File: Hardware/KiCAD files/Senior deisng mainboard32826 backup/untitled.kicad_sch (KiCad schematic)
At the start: 2 parts, among them U4 ESP32-S3-WROOM-2, U9 ESP32-S3-DevKitC

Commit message: Schematic adjustments made prior to initial submission to Chan thursday
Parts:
- removed U4: ESP32-S3-WROOM-2, PCM_Espressif:ESP32-S3-WROOM-2, symbol PCM_Espressif:ESP32-S3-WROOM-2
- removed U9: ESP32-S3-DevKitC, PCM_Espressif:ESP32-S3-DevKitC, symbol PCM_Espressif:ESP32-S3-DevKitC
- added J3: Rasberry Uart Conn_01x02, PCM_SparkFun-Connector:1x02_P2.54mm, symbol PCM_SparkFun-Connector:Conn_01x02_P2.54mm
- added U4: STM32H750VBTx, Package_QFP:LQFP-100_14x14mm_P0.5mm, symbol PCM_SparkFun-IC-Microcontroller:STM32H750VBTx
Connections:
- new net: U4.10 (VSS), U4.26 (VSS), U4.49 (VSS), U4.74 (VSS), U4.99 (VSS)
- new net VDD: U4.100 (VDD), U4.11 (VDD), U4.27 (VDD), U4.50 (VDD), U4.75 (VDD)

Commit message: MCU power, new MCU placed, LCD communication, AC coupling of voltage reg on MCU
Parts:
- removed U4: STM32H750VBTx, Package_QFP:LQFP-100_14x14mm_P0.5mm, symbol PCM_SparkFun-IC-Microcontroller:STM32H750VBTx
- added C13: 10uF, PCM_SparkFun-Capacitor:C_0805_2012Metric, symbol PCM_SparkFun-Capacitor:10uF_0805_25V_10%
- added C14: 0.1uF, PCM_SparkFun-Capacitor:C_0603_1608Metric, symbol PCM_SparkFun-Capacitor:0.1uF_0603_25V_20%
- added C16: 1.0uF, PCM_SparkFun-Capacitor:C_0402_1005Metric, symbol PCM_SparkFun-Capacitor:1.0uF_0402_16V_10%
- added IC1: STM32H723ZGT6, QFP50P2200X2200X160-144N, symbol STM32H723ZGT6:STM32H723ZGT6
- added SW5: SPDT_Slide_PTH_11.6x4.0mm, PCM_SparkFun-Switch:Slide_SPDT_PTH_11.6x4.0mm, symbol PCM_SparkFun-Switch:SPDT_Slide_PTH_11.6x4.0mm
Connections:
- net LPUART_RX: now reaches J3.1 (Pin_1)
- net LPUART_RX: now also IC1.102 (PA10)
- net LPUART_TX: now reaches J3.2 (Pin_2)
- net LPUART_TX: now also IC1.101 (PA9)
- new net: C13.2, C14.2
- new net +3.3V: C13.1, C14.1, C16.2, IC1.108 (VDD_8), IC1.121 (VDD_9), IC1.131 (VDD_10), IC1.144 (VDD_11), IC1.17 (VDD_1), IC1.30 (VDD_2), IC1.32 (VREF+), IC1.33 (VDDA), IC1.39 (VDD_3), IC1.52 (VDD_4), IC1.6 (VBAT), IC1.62 (VDD_5), IC1.72 (VDD_6), IC1.84 (VDD_7)
- new net CS: IC1.28 (PC2_C)
- new net GND: C16.1, IC1.107 (VSS_7), IC1.120 (VSS_8), IC1.130 (VSS_9), IC1.16 (VSS_1), IC1.31 (VSSA), IC1.38 (VSS_2), IC1.51 (VSS_3), IC1.61 (VSS_4), IC1.83 (VSS_5), IC1.94 (VSS_6)
- new net LCD_CLK: IC1.67 (PE14)
- new net MISO_4: IC1.4 (PE5)
- new net MOSI_4: IC1.5 (PE6)
- new net SPI4_SCK: IC1.1 (PE2)
- no-connect marks 0 -> 2
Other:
- note added: "100ma max"
- note added: "20ma max gpio"
- note added: "AC COUPPLING --- may not be neccesary"
- note added: "COME BACK AND VERIFY VOLTAGE REGULATION OF EACH POWER INPUT VDD_X"
- note added: "KEEP VREF+ and VSSA cap as close as possible to chip"
- note added: "PDR_on is for voltage supervision, meant for low power applications"
- note added: "Reset switch"
- note added: "Supply rail must have 10 us/V fall time"
- note added: "VBAT pin should be connected to VDD."
- note added: "VDD33USB: allows the support of a VDD supply different from 3.3 V while powering the USB transceiver with 3.3V on VDD33USB."
- note added: "check if VDDA needs a diff voltage regulation"
- note added: "introduces voltage scaling and powering Vcore @ Vcap"
- moved on the sheet: J3

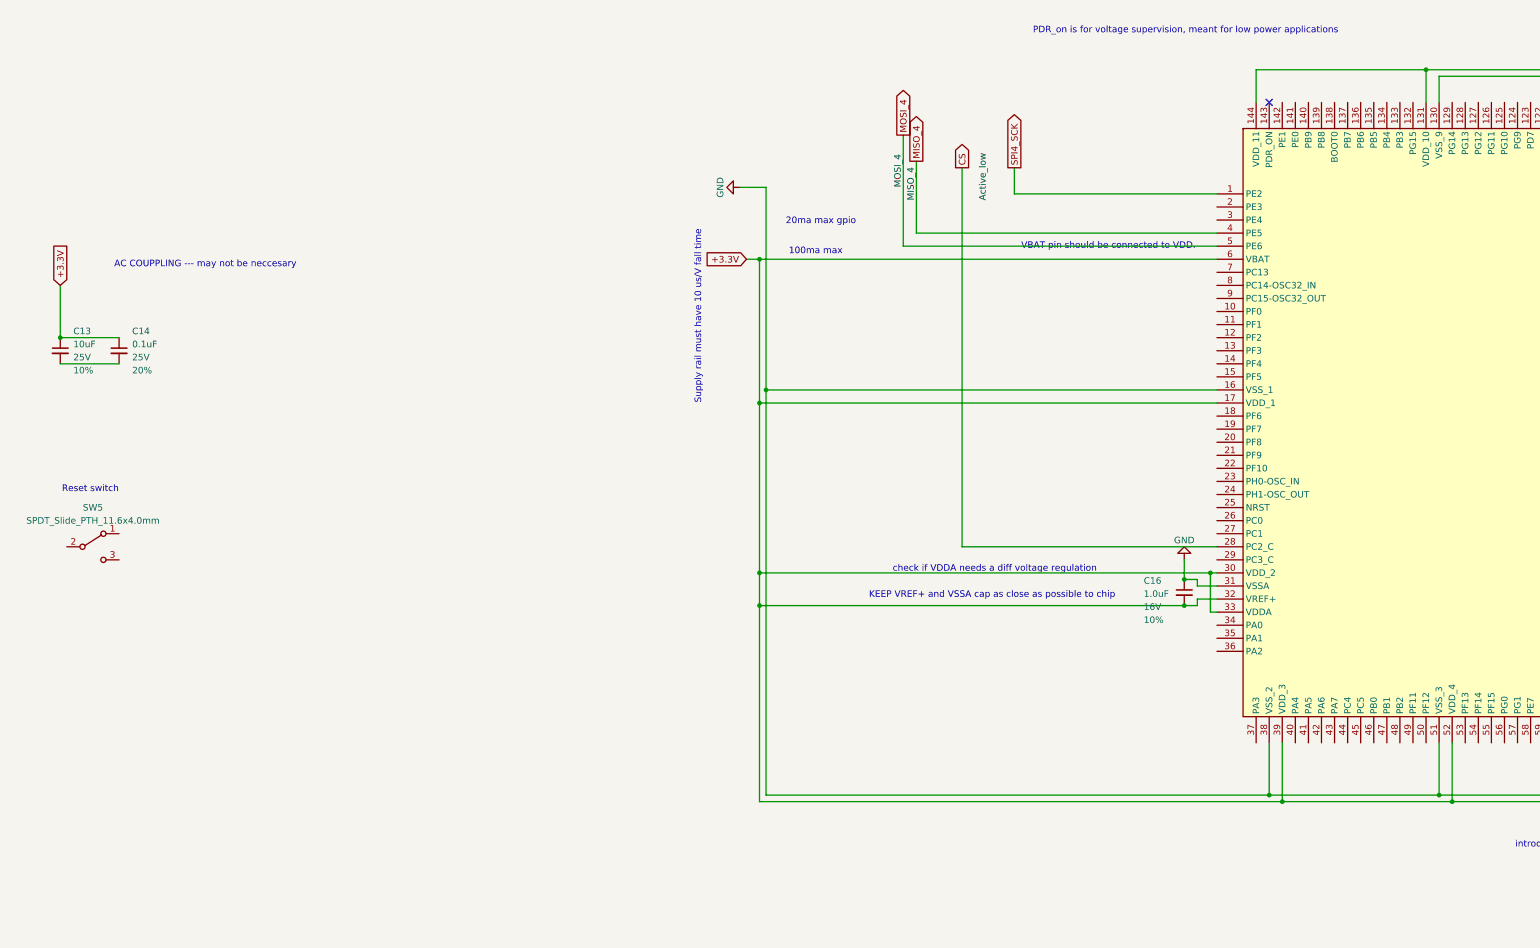
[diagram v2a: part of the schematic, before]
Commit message: IO pull resistors, Motor driver V1, LCD communication
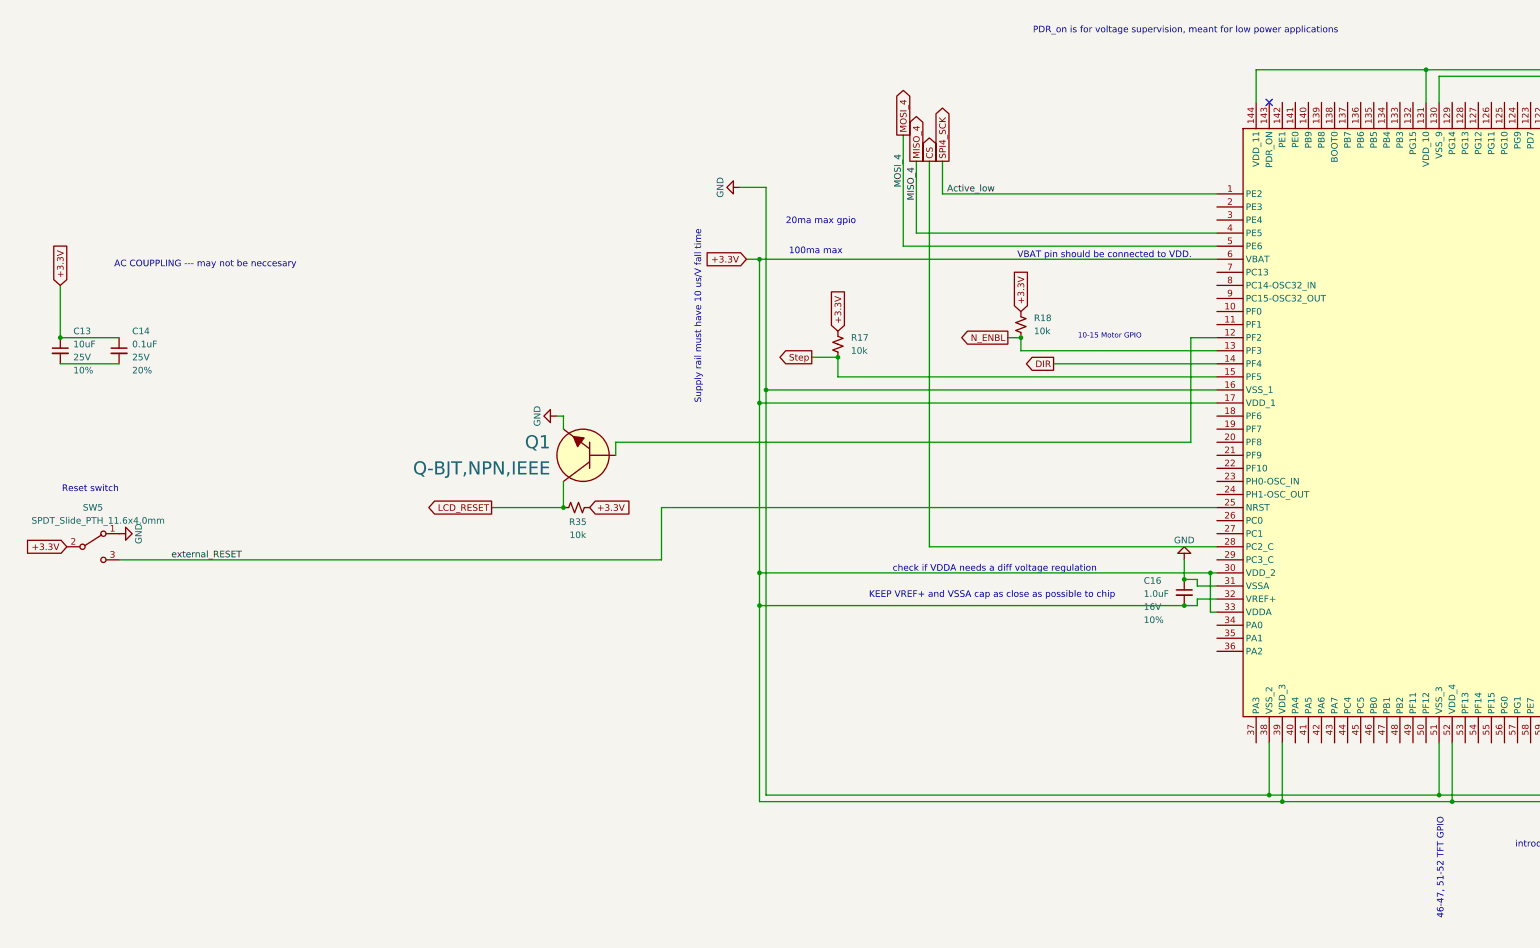
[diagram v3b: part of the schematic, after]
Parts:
- added Q1: Q-BJT,NPN,IEEE, symbol PCM_Generic:Q-BJT,NPN,IEEE
- added R17, R18, R35: 10k, PCM_SparkFun-Resistor:R_0603_1608Metric, symbol PCM_SparkFun-Resistor:10k_0603
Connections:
- net +3.3V: now also SW5.2 (B), R17.2, R18.2, R35.1
- net GND: now also SW5.1 (A), Q1.3 (E)
- net at IC1.12 (PF2): now also Q1.2 (B)
- net N_ENBL: now reaches IC1.13 (PF3)
- net N_ENBL: now also R18.1
- net DIR: now reaches IC1.14 (PF4)
- net Step: now reaches IC1.15 (PF5)
- net Step: now also R17.1
- net external_RESET: now reaches IC1.25 (NRST)
- net external_RESET: now also SW5.3 (C)
- new net LCD_RESET: Q1.1 (C), R35.2
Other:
- note added: "10-15 Motor GPIO"
- note added: "46-47, 51-52 TFT GPIO"

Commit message: 1.1, devices have been cleaned up
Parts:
- removed J3: Rasberry Uart Conn_01x02, PCM_SparkFun-Connector:1x02_P2.54mm, symbol PCM_SparkFun-Connector:Conn_01x02_P2.54mm
- added C49: 0.1uF, PCM_SparkFun-Capacitor:C_0603_1608Metric, symbol PCM_SparkFun-Capacitor:0.1uF_0603_25V_20%
- added J23: Conn_01x02, PCM_SparkFun-Connector:1x02_P2.54mm, symbol PCM_SparkFun-Connector:Conn_01x02_P2.54mm
- added J25: JST_1mm_3_Vertical, PCM_SparkFun-Connector:JST_1x03_P1.0mm_Vertical_SMD, symbol PCM_SparkFun-Connector:Conn_01x03_JST_P1.0mm_Vertical_SMD
- added J27: Conn_01x04, PCM_SparkFun-Connector:1x04_P2.54mm, symbol PCM_SparkFun-Connector:Conn_01x04_P2.54mm
- added Q2, Q3: Q-BJT,NPN,IEEE, symbol PCM_Generic:Q-BJT,NPN,IEEE
- added R44: 10k, PCM_SparkFun-Resistor:R_0603_1608Metric, symbol PCM_SparkFun-Resistor:10k_0603
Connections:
- net +3.3V: now also J25.3, Q2.1 (C), R44.2
- net GND: now also C49.2, J25.2, J27.4 (Pin_4)
- net LPUART_RX: now also J27.1 (Pin_1)
- net LPUART_TX: now also J27.2 (Pin_2)
- net external_RESET: now also C49.1
- net E_Step: now reaches IC1.10 (PF0)
- net E_Step: now also R44.1
- net DATA_SELECT: now reaches IC1.11 (PF1)
- net TEMP_HOTPLATE: now reaches IC1.49 (PF11)
- net at IC1.70 (PB11): now also J25.1
- net at IC1.74 (PB13): now also Q3.3 (E)
- net MODE_2_GPIO: now reaches IC1.87 (PG2)
- net MODE_1_GPIO: now reaches IC1.88 (PG3)
- net MODE_0_GPIO: now reaches IC1.89 (PG4)
- net MODE_2_GPIOE: now reaches IC1.90 (PG5)
- net MODE_1_GPIOE: now reaches IC1.91 (PG6)
- net MODE_0_GPIOE: now reaches IC1.92 (PG7)
- net CS renamed SPI4_CS
- net LCD_CLK: no longer names the net of IC1.67 (PE14)
- new net: Q2.3 (E), Q3.1 (C)
- new net: J23.1 (Pin_1), Q3.2 (B)
- new net: J23.2 (Pin_2), Q2.2 (B)
- new net +5V_HIGHPW: J27.3 (Pin_3)
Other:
- note added: "+3.3V,GND, Z-Switch in that order from Gantry side board"
- note added: "87-93 gpio"
- note added: "ADC 16-bit"
- note added: "Z-Switch"
- note added: "clock"
- note added: "drivers"
- note added: "open GPIO"
- note added: "test that reset drops below 1.62 Volts between presses"
- note added: "verify that the voltage does not drop too much from the head"
- note removed: "46-47, 51-52 TFT GPIO"
- moved on the sheet: R17

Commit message: swapping connectors and rewiring through the project.
we verified connections with the ender3. a few placeholders replaced.
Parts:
- removed C13: 10uF, PCM_SparkFun-Capacitor:C_0805_2012Metric, symbol PCM_SparkFun-Capacitor:10uF_0805_25V_10%
- removed C14: 0.1uF, PCM_SparkFun-Capacitor:C_0603_1608Metric, symbol PCM_SparkFun-Capacitor:0.1uF_0603_25V_20%
- removed Q2: Q-BJT,NPN,IEEE, symbol PCM_Generic:Q-BJT,NPN,IEEE
- added C2: 10uF, PCM_SparkFun-Capacitor:C_1210_3225Metric, symbol PCM_SparkFun-Capacitor:10uF_1210_50V_20%
- added J32: JST_03, Connector_JST:JST_EH_B3B-EH-A_1x03_P2.50mm_Vertical, symbol PCM_SL_Connectors:JST_03
- added J33: Conn_01x04, PCM_SparkFun-Connector:1x04_P2.54mm, symbol PCM_SparkFun-Connector:Conn_01x04_P2.54mm
- added R48, R49, R50: 10k, PCM_SparkFun-Resistor:R_0603_1608Metric, symbol PCM_SparkFun-Resistor:10k_0603
- added R5: 10k, Resistor_THT:R_Axial_DIN0207_L6.3mm_D2.5mm_P10.16mm_Horizontal, symbol PCM_SL_Resistors:10k
- added SW8, SW9: Push_Button, Button_Switch_THT:SW_PUSH_6mm, symbol PCM_SL_Devices:Push_Button
- added U12: ESP32-S3-WROOM-1, PCM_Espressif:ESP32-S3-WROOM-1, symbol PCM_Espressif:ESP32-S3-WROOM-1
- IC1: footprint QFP50P2200X2200X160-144N -> (none)
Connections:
- net +3.3V: now also C2.1, J32.3, R48.1, R49.2, R5.1, R50.2, U12.2 (3V3)
- net +5V_HIGHPW: now also J33.3 (Pin_3)
- net DATA_SELECT: now also U12.23 (GPIO21)
- net DIR: now also U12.16 (GPIO46)
- net GND: now also Q3.3 (E), C2.2, J32.2, J33.4 (Pin_4), SW9.2, U12.1 (GND), U12.40 (GND), U12.41 (GND)
- net LCD_RESET: now also Q3.1 (C), R48.2
- net MISO_4: now also U12.30 (SPIDQS/GPIO37/FSPIQ/SUBSPIQ)
- net MODE_0_GPIO: now also U12.5 (GPIO5/TOUCH5/ADC1_CH4)
- net MODE_0_GPIOE: now also U12.38 (GPIO2/TOUCH2/ADC1_CH1)
- net MODE_1_GPIO: now also U12.6 (GPIO6/TOUCH6/ADC1_CH5)
- net MODE_1_GPIOE: now also U12.15 (GPIO3/TOUCH3/ADC1_CH2)
- net MODE_2_GPIO: now also U12.7 (GPIO7/TOUCH7/ADC1_CH6)
- net MODE_2_GPIOE: now also U12.4 (GPIO4/TOUCH4/ADC1_CH3)
- net MOSI_4: now also U12.28 (SPIIO6/GPIO35/FSPID/SUBSPID)
- net N_ENBL: now also R49.1, U12.26 (GPIO45)
- net SPI4_CS: now also U12.18 (GPIO10/TOUCH10/ADC1_CH9/FSPICS0/FSPIIO4/SUBSPICS0)
- net SPI4_SCK: now also U12.29 (SPIIO7/GPIO36/FSPICLK/SUBSPICLK)
- net Step: now also R50.1, U12.12 (GPIO8/TOUCH8/ADC1_CH7/SUBSPICS1)
- net TEMP_HOTPLATE: now also U12.39 (GPIO1/TOUCH1/ADC1_CH0)
- net at IC1.73 (PB12): now also J23.1 (Pin_1)
- net at IC1.74 (PB13): now also J23.2 (Pin_2); no longer Q3.3 (E)
- net at Q3.2 (B): now also U12.31 (GPIO38/FSPIWP/SUBSPIWP); no longer J23.1 (Pin_1)
- new net: R5.2, SW8.2
- new net: J33.1 (Pin_1), U12.10 (GPIO17/U1TXD/ADC2_CH6)
- new net: J33.2 (Pin_2), U12.11 (GPIO18/U1RXD/ADC2_CH7/CLK_OUT3)
- new net: J32.1, U12.35 (MTMS/GPIO42)
- new net: SW8.1, U12.3 (EN)
- new net: SW9.1, U12.27 (GPIO0/BOOT)
- new net D+: U12.14 (GPIO20/U1CTS/ADC2_CH9/CLK_OUT1/USB_D+)
- new net D-: U12.13 (GPIO19/U1RTS/ADC2_CH8/CLK_OUT2/USB_D-)
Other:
- note removed: "AC COUPPLING --- may not be neccesary"
- note removed: "open GPIO"
- moved on the sheet: C16, C49, IC1, J23, J25, J27, Q1, R17, R18, R35, R44, SW5

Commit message: New project made to reflect layouts
New project files made in order to generate accurate layouts and create neatness.
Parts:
- removed C16: 1.0uF, PCM_SparkFun-Capacitor:C_0402_1005Metric, symbol PCM_SparkFun-Capacitor:1.0uF_0402_16V_10%
- removed C49: 0.1uF, PCM_SparkFun-Capacitor:C_0603_1608Metric, symbol PCM_SparkFun-Capacitor:0.1uF_0603_25V_20%
- removed IC1: STM32H723ZGT6, symbol STM32H723ZGT6:STM32H723ZGT6
- removed J23: Conn_01x02, PCM_SparkFun-Connector:1x02_P2.54mm, symbol PCM_SparkFun-Connector:Conn_01x02_P2.54mm
- removed J25: JST_1mm_3_Vertical, PCM_SparkFun-Connector:JST_1x03_P1.0mm_Vertical_SMD, symbol PCM_SparkFun-Connector:Conn_01x03_JST_P1.0mm_Vertical_SMD
- removed J27: Conn_01x04, PCM_SparkFun-Connector:1x04_P2.54mm, symbol PCM_SparkFun-Connector:Conn_01x04_P2.54mm
- removed Q1, Q3: Q-BJT,NPN,IEEE, symbol PCM_Generic:Q-BJT,NPN,IEEE
- removed R17, R18, R35, R44: 10k, PCM_SparkFun-Resistor:R_0603_1608Metric, symbol PCM_SparkFun-Resistor:10k_0603
- removed SW5: SPDT_Slide_PTH_11.6x4.0mm, PCM_SparkFun-Switch:Slide_SPDT_PTH_11.6x4.0mm, symbol PCM_SparkFun-Switch:SPDT_Slide_PTH_11.6x4.0mm
- added C16: 0.1uF, PCM_SparkFun-Capacitor:C_0603_1608Metric, symbol PCM_SparkFun-Capacitor:0.1uF_0603_25V_20%
- added D9: LED, LED_SMD:LED_0603_1608Metric, symbol Device:LED
- added J1: Conn_01x02, PCM_SparkFun-Connector:1x02_P2.54mm, symbol PCM_SparkFun-Connector:Conn_01x02_P2.54mm
- added Q2: 2DD1664, PCM_Package_TO_SOT_SMD_AKL:SOT-89-3, symbol PCM_Transistor_BJT_AKL:2DD1664
- added R36: 1k, Resistor_SMD:R_1206_3216Metric_Pad1.30x1.75mm_HandSolder, symbol Device:R_US
- added R51, R52, R53, R55: 10k, PCM_SparkFun-Resistor:R_0603_1608Metric, symbol PCM_SparkFun-Resistor:10k_0603
- added U3: PCA9534PW, PCM_SparkFun-Semiconductor-Standard:TSSOP-16_4.4x5mm_P0.65mm, symbol PCM_SparkFun-IC-Special-Function:PCA9534PW
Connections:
- net +3.3V: now also C16.1, R36.1, R51.1, R52.2, R53.2, R55.1, U3.8 (VSS)
- net GND: now also C16.2, D9.1 (K), Q2.3 (E), U3.1 (A0), U3.16 (VDD), U3.2 (A1)
- net LCD_RESET: now also Q2.2 (C)
- net MODE_0_GPIO: now also U3.6 (IO2); no longer U12.5 (GPIO5/TOUCH5/ADC1_CH4)
- net MODE_0_GPIOE: now also U3.10 (IO5); no longer U12.38 (GPIO2/TOUCH2/ADC1_CH1)
- net MODE_1_GPIO: now also U3.5 (IO1); no longer U12.6 (GPIO6/TOUCH6/ADC1_CH5)
- net MODE_1_GPIOE: now also U3.9 (IO4); no longer U12.15 (GPIO3/TOUCH3/ADC1_CH2)
- net MODE_2_GPIO: now also U3.4 (IO0); no longer U12.7 (GPIO7/TOUCH7/ADC1_CH6)
- net MODE_2_GPIOE: now also U3.7 (IO3); no longer U12.4 (GPIO4/TOUCH4/ADC1_CH3)
- net Step: now also U12.4 (GPIO4/TOUCH4/ADC1_CH3); no longer U12.12 (GPIO8/TOUCH8/ADC1_CH7/SUBSPICS1)
- net at J32.1: now also U3.11 (IO6); no longer U12.35 (MTMS/GPIO42)
- net at U12.31 (GPIO38/FSPIWP/SUBSPIWP): now also Q2.1 (B)
- net MISO_1: now reaches U12.19 (GPIO11/TOUCH11/ADC2_CH0/FSPID/FSPIIO5/SUBSPID)
- net SPI1_CLK: now reaches U12.20 (GPIO12/TOUCH12/ADC2_CH1/FSPICLK/FSPIIO6/SUBSPICLK)
- net MOSI_1: now reaches U12.21 (GPIO13/TOUCH13/ADC2_CH2/FSPIQ/FSPIIO7/SUBSPIQ)
- net at U12.36 (U0RXD/GPIO44/CLK_OUT2): now also J1.2 (Pin_2)
- net at U12.37 (U0TXD/GPIO43/CLK_OUT1): now also J1.1 (Pin_1)
- net at U12.8 (GPIO15/U0RTS/ADC2_CH4/XTAL_32K_P): now also R53.1, U3.15 (SDA)
- net at U12.9 (GPIO16/U0CTS/ADC2_CH5/XTAL_32K_N): now also R52.1, U3.14 (SCL)
- net SPI4_SCK renamed SPI4_CLK
- new net: R51.2, U3.3 (A2)
- new net: D9.2 (A), R36.2
- new net 3.3V_in1: U12.15 (GPIO3/TOUCH3/ADC1_CH2)
- new net AXIS_E_ENDSTOP: U3.12 (IO7)
- new net AXIS_X_ENDSTOP: U12.6 (GPIO6/TOUCH6/ADC1_CH5)
- new net AXIS_Y_ENDSTOP: U12.5 (GPIO5/TOUCH5/ADC1_CH4)
- new net IO_Interupter: R55.2, U12.38 (GPIO2/TOUCH2/ADC1_CH1), U3.13 (~{INT})
- new net SPI1_CS: U12.12 (GPIO8/TOUCH8/ADC1_CH7/SUBSPICS1)
- no-connect marks 2 -> 0
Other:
- note added: "I2C lanes"
- note added: "verify that esp interrupt is on this pin"
- note removed: "+3.3V,GND, Z-Switch in that order from Gantry side board"
- note removed: "10-15 Motor GPIO"
- note removed: "100ma max"
- note removed: "20ma max gpio"
- note removed: "87-93 gpio"
- note removed: "ADC 16-bit"
- note removed: "COME BACK AND VERIFY VOLTAGE REGULATION OF EACH POWER INPUT VDD_X"
- note removed: "KEEP VREF+ and VSSA cap as close as possible to chip"
- note removed: "PDR_on is for voltage supervision, meant for low power applications"
- note removed: "Reset switch"
- note removed: "Supply rail must have 10 us/V fall time"
- note removed: "VBAT pin should be connected to VDD."
- note removed: "VDD33USB: allows the support of a VDD supply different from 3.3 V while powering the USB transceiver with 3.3V on VDD33USB."
- note removed: "check if VDDA needs a diff voltage regulation"
- note removed: "clock"
- note removed: "introduces voltage scaling and powering Vcore @ Vcap"
- note removed: "test that reset drops below 1.62 Volts between presses"
- note removed: "verify that the voltage does not drop too much from the head"
- moved on the sheet: J32, J33, R48, R50
